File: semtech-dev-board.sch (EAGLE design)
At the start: 59 parts, among them Q1 BSS123, U1 MIC5219 3.3V, U2 QUALCOMM-TDK_B3710, U3 QUALCOMM-TDK_B3588, U4 SEMTECH_SX1236, Y1 32MHz

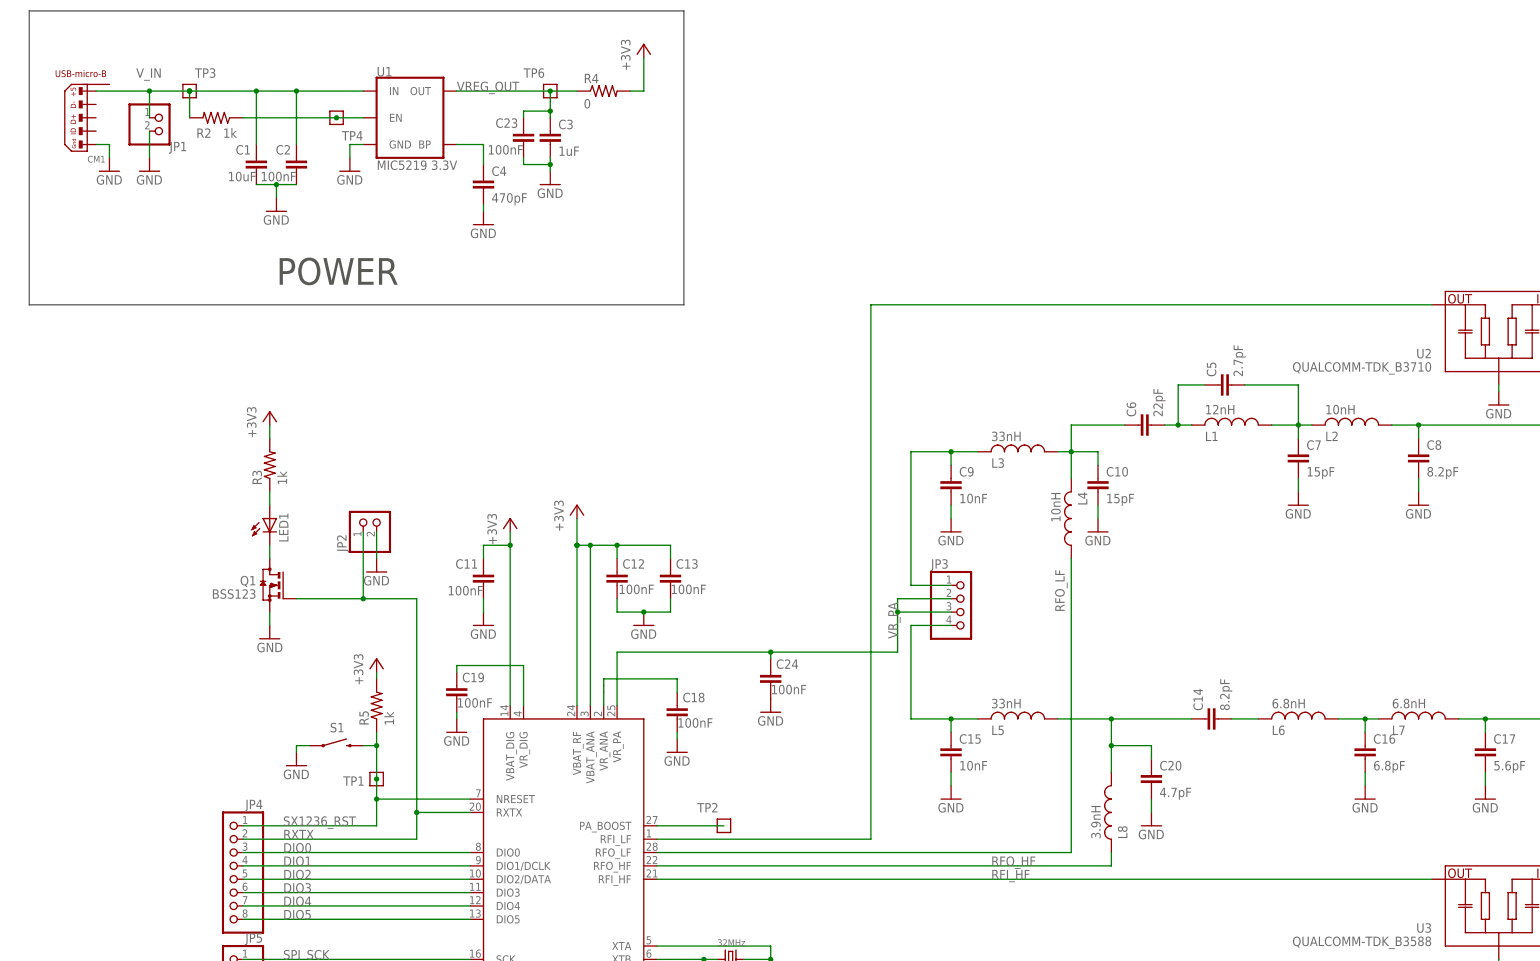
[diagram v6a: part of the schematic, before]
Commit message: Chose parts and added Digikey part numbers to BoM, switched inductors to 0603 because it was easy, shrunk board by 3 mm, cleaned up stapling, switched LEDs to 0603, oh and added a power LED for fun.
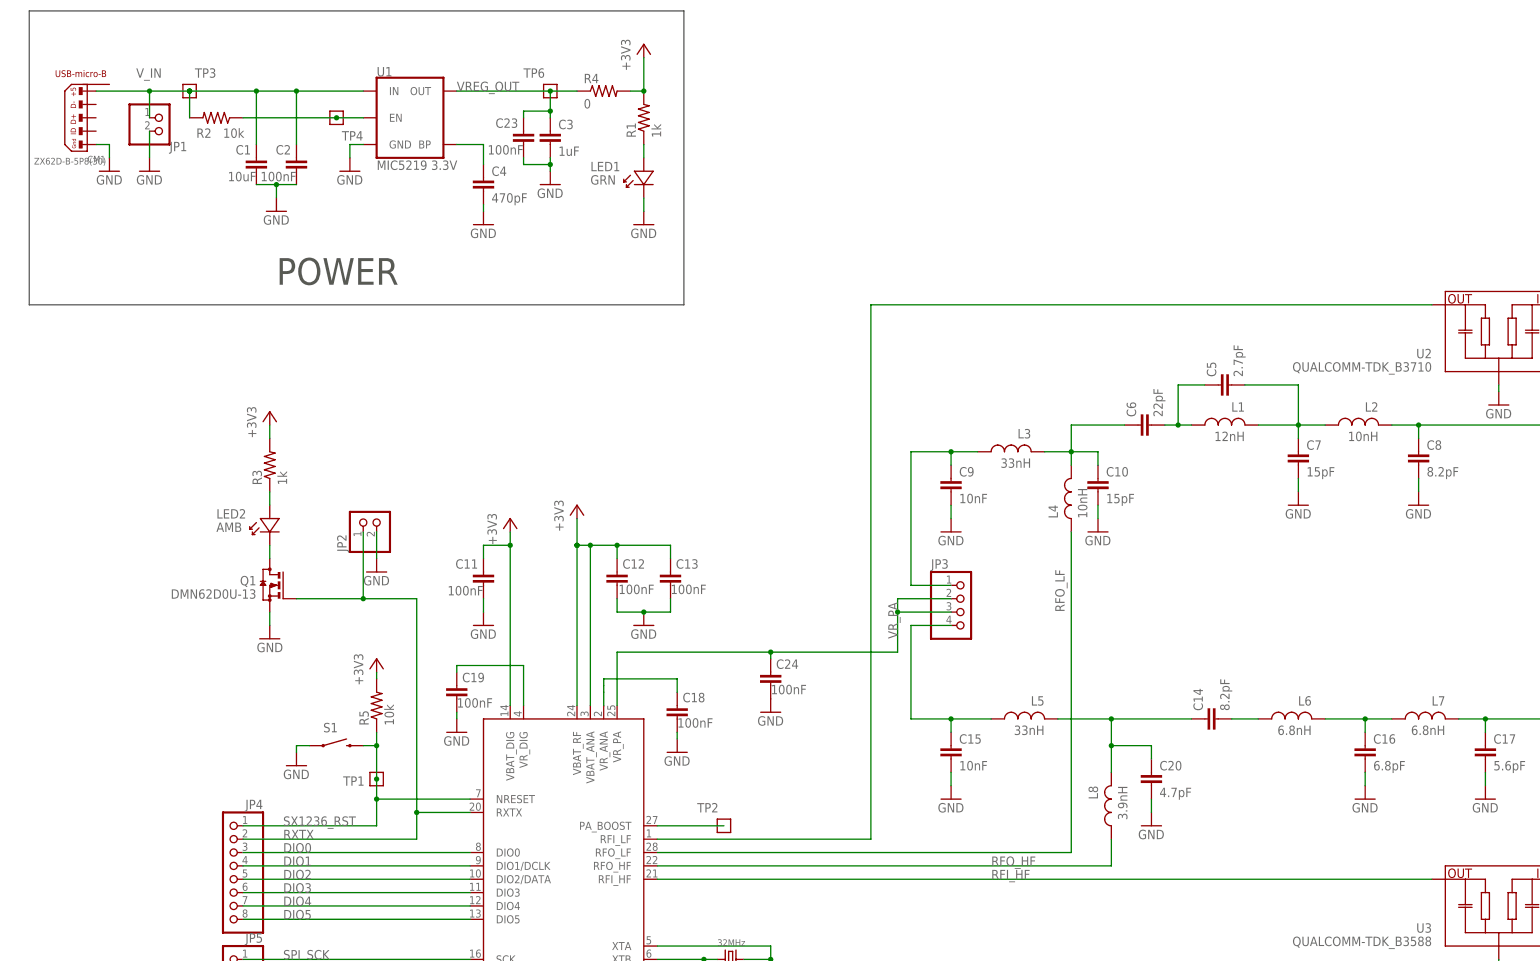
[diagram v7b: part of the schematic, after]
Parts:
- added LED2: AMB, low-gain-radio:LED-0603
- added R1: 1k, rcl_custom:R-US_0603-B-NOSILK
- CM1: value (none) -> ZX62D-B-5P8(30)
- L1, L2, L3, L4, L5, L6, L7, L8: device rcl:L-USL3225M -> rcl_custom:L-US0603-B-NOSILK
- LED1: value (none) -> GRN; device led:LEDCHIP-LED0805 -> low-gain-radio:LED-0603
- Q1: value BSS123 -> DMN62D0U-13
- R2, R5: value 1k -> 10k
- S1: value SWITCH-MOMENTARY-2SMD-2 -> FSM4JSMATR
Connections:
- new net N$5: LED1.A, R1.1
- net +3V3: now also R1.2
- net GND: now also LED1.K
- net LED+: now also LED2.A; no longer LED1.A
- net LED-: now also LED2.K; no longer LED1.C

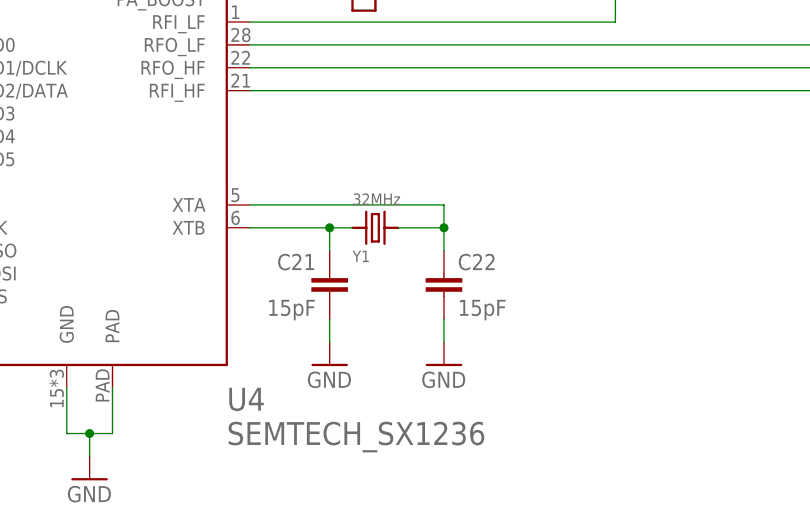
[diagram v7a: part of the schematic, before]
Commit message: Whoah - almost missed the fixed to the crystal from the LGR board. Kenny would have totally killed us all.
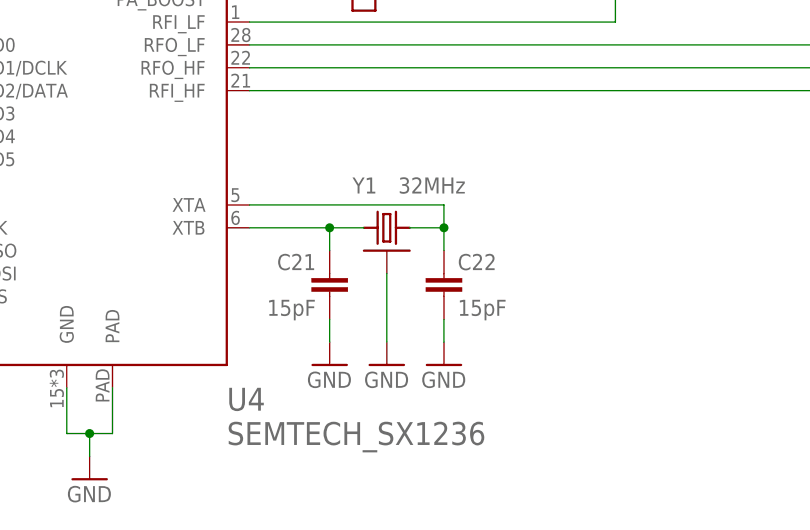
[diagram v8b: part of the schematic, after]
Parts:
- Y1: device low-gain-radio:CRYSTAL2.5X2.0MM -> low-gain-radio:CRYSTAL-WITH-GND
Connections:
- net GND: now also Y1.SHIELD
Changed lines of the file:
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@@
 <setting verticaltext="up"/>
 </settings>
-<grid distance="0.1" unitdist="inch" unit="inch" style="lines" multiple="1" display="no" altdistance="0.01" altunitdist="inch" altunit="inch"/>
+<grid distance="0.05" unitdist="inch" unit="inch" style="lines" multiple="1" display="no" altdistance="0.01" altunitdist="inch" altunit="inch"/>
 <layers>
 <layer number="1" name="Top" color="4" fill="1" visible="no" active="no"/>
@@
 <parts>
 <part name="JP4" library="pinhead" library_urn="urn:adsk.eagle:library:325" deviceset="PINHD-1X8" device=""/>
-<part name="Y1" library="low-gain-radio" deviceset="CRYSTAL" device="2.5X2.0MM" value="32MHz"/>
+<part name="Y1" library="low-gain-radio" deviceset="CRYSTAL-WITH-GND" device="" value="32MHz"/>
 <part name="GND22" library="supply1" deviceset="GND" device=""/>
 <part name="Q1" library="transistor-small-signal" library_urn="urn:adsk.eagle:library:401" deviceset="BSS123" device="" value="DMN62D0U-13"/>
@@
 <part name="LED1" library="low-gain-radio" deviceset="LED" device="-0603" value="GRN"/>
 <part name="LED2" library="low-gain-radio" deviceset="LED" device="-0603" value="AMB"/>
+<part name="GND33" library="supply1" deviceset="GND" device=""/>
 </parts>
 <sheets>
@@
 <instances>
 <instance part="JP4" gate="A" x="68.58" y="81.28" rot="MR0"/>
-<instance part="Y1" gate="G$1" x="163.83" y="66.04" rot="MR180"/>
+<instance part="Y1" gate="G$1" x="165.1" y="66.04" smashed="yes">
+<attribute name="NAME" x="161.29" y="69.85" size="1.778" layer="95"/>
+<attribute name="VALUE" x="166.37" y="69.85" size="1.778" layer="96"/>
+</instance>
 <instance part="GND22" gate="1" x="81.28" y="102.87"/>
 <instance part="Q1" gate="G$1" x="76.2" y="137.16" rot="MR0"/>
@@
 <attribute name="VALUE" x="66.04" y="147.32" size="1.778" layer="96"/>
 </instance>
+<instance part="GND33" gate="1" x="165.1" y="50.8"/>
 </instances>
 <busses>
@@
 <pinref part="LED1" gate="LED" pin="K"/>
 </segment>
+<segment>
+<pinref part="GND33" gate="1" pin="GND"/>
+<pinref part="Y1" gate="G$1" pin="SHIELD"/>
+<wire x1="165.1" y1="53.34" x2="165.1" y2="60.96" width="0.1524" layer="91"/>
+</segment>
 </net>
 <net name="SPI_NSS" class="0">
@@
 <wire x1="158.75" y1="66.04" x2="149.86" y2="66.04" width="0.1524" layer="91"/>
 <pinref part="Y1" gate="G$1" pin="1"/>
-<wire x1="158.75" y1="66.04" x2="161.29" y2="66.04" width="0.1524" layer="91"/>
+<wire x1="158.75" y1="66.04" x2="162.56" y2="66.04" width="0.1524" layer="91"/>
 <pinref part="C21" gate="CE" pin="1"/>
 <wire x1="158.75" y1="63.5" x2="158.75" y2="66.04" width="0.1524" layer="91"/>
@@
 <wire x1="171.45" y1="68.58" x2="171.45" y2="66.04" width="0.1524" layer="91"/>
 <pinref part="C22" gate="CE" pin="1"/>
-<wire x1="171.45" y1="66.04" x2="166.37" y2="66.04" width="0.1524" layer="91"/>
+<wire x1="171.45" y1="66.04" x2="167.64" y2="66.04" width="0.1524" layer="91"/>
 <wire x1="171.45" y1="63.5" x2="171.45" y2="66.04" width="0.1524" layer="91"/>
 <junction x="171.45" y="66.04"/>
